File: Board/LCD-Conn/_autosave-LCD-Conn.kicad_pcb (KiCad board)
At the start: 2 copper layers, 37.8 x 20 mm, 2 parts, among them J1 Conn_LCD, J2 Conn_Board

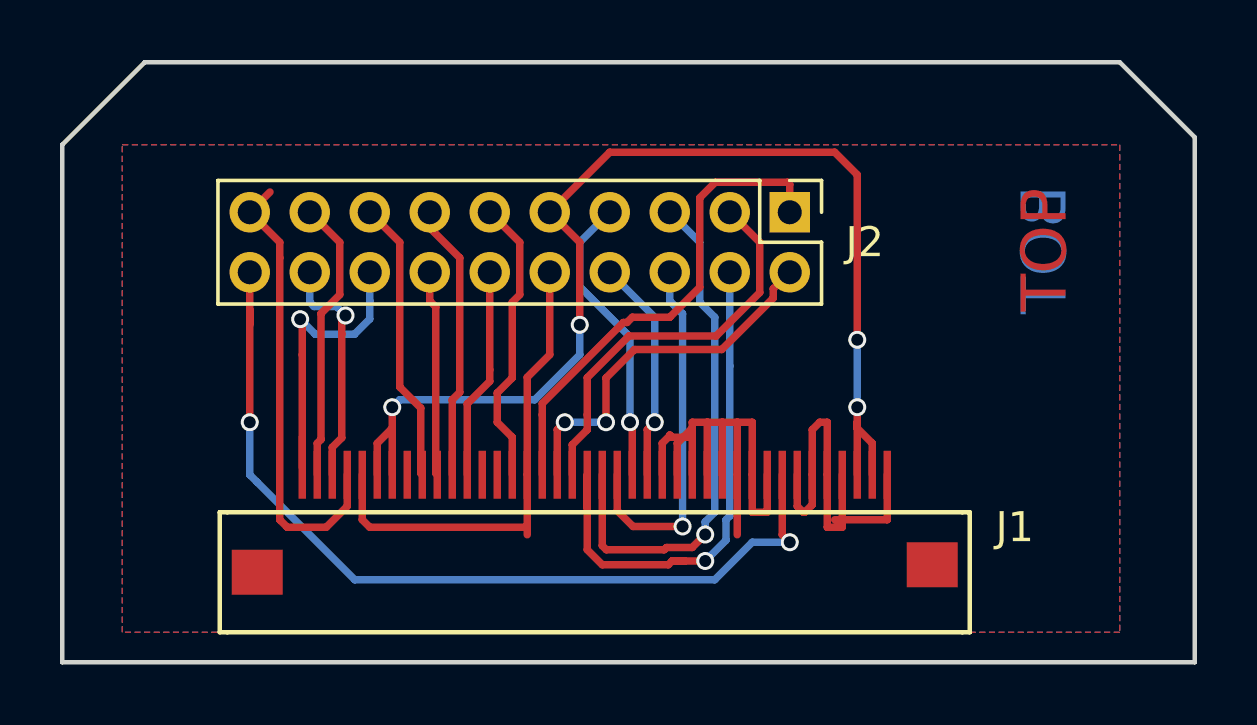
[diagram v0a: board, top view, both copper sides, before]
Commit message: Board: SD slot moved, usb-conn changed from slots to holes. LCD board polished. Repo cleaned up.
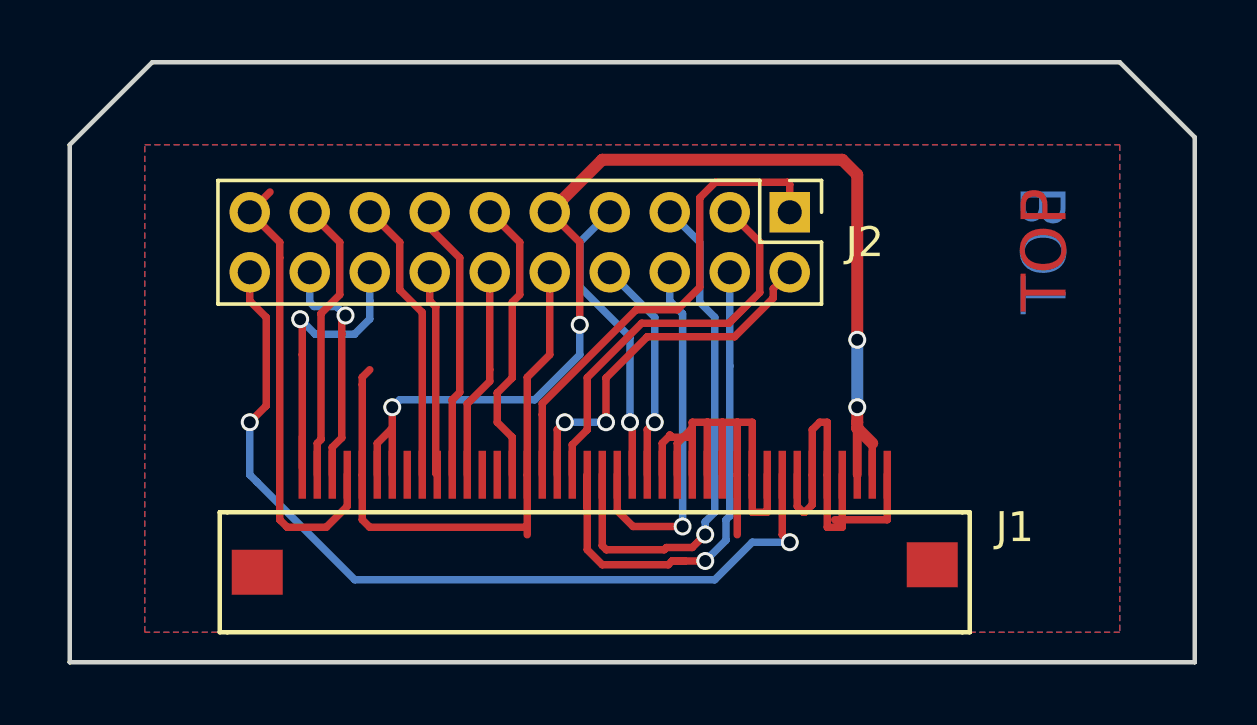
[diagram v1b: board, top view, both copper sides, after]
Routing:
- net GND: track 49.7 -> 53.3 mm
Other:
- board size 37.8 x 20 mm -> 37.5 x 20 mm
